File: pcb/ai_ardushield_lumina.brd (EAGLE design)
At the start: 69.8 x 53.3 mm, 90 parts, among them J1 1X02ST, J2 1X01, J3 1X06, J4 1X08, J5 1X08, J6 1X10, SW1 SW-SPST, U1 ARDUINOUNOR3-STRAIGHT

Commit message: Updated to latest libraries.  New Gerbers.
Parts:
- removed SW1: SW-SPST, Ai_Electromechanical:SPST-SMD
- added S1: SW-SPSTSMD06X06, Ai_Electromechanical:SPST-SMD06X06
- C1, C10, C11, C12, C13, C14, C15, C16, C17, C18, C19, C2, C20, C21, C22, C23, C24, C25, C26, C27, C28, C29, C3, C30, C31, C32, C33, C34, C35, C36, C37, C38, C39, C4, C40, C5, C6, C7, C8, C9: value (none) -> 0.1uF; device Ai_Passives:0603-CAP -> Ai_Passives:CAP-0603
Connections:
- net GND: now also S1.A@1, S1.A@2; no longer C38.2, SW1.A@1, SW1.A@2
- net RST: now also S1.B@1, S1.B@2; no longer SW1.B@1, SW1.B@2
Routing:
- net GND: track 532.3 -> 488.7 mm
- net RST: track 99.5 -> 91.6 mm

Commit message: Modified the routing quite a bit.
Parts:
- S1: device Ai_Electromechanical:SPST-SMD06X06 -> Ai_Electromechanical:SW-SPST-SMD06X06
- moved C13 3.43 mm to (30.4, 38.4), flipped to the top, turned to 180 degrees
- moved C10 3.43 mm to (57.1, 38.4), flipped to the top, turned to 180 degrees
- moved C11 3.43 mm to (48.3, 38.4), flipped to the top, turned to 180 degrees
- moved C12 3.43 mm to (39.4, 38.4), flipped to the top, turned to 180 degrees
- moved C14 3.43 mm to (21.6, 38.4), flipped to the top, turned to 180 degrees
- moved C15 3.43 mm to (12.7, 38.4), flipped to the top, turned to 180 degrees
- moved C16 3.43 mm to (3.81, 38.4), flipped to the top, turned to 180 degrees
- moved C9 3.43 mm to (66.0, 38.4), flipped to the top, turned to 180 degrees
- moved C17 3.30 mm to (3.81, 30.0), flipped to the top, turned to 180 degrees
- moved C18 3.30 mm to (12.7, 30.0), flipped to the top, turned to 180 degrees
- moved C19 3.30 mm to (21.6, 30.0), flipped to the top, turned to 180 degrees
- moved C20 3.30 mm to (30.5, 30.0), flipped to the top, turned to 180 degrees
- moved C21 3.30 mm to (39.4, 30.0), flipped to the top, turned to 180 degrees
- moved C22 3.30 mm to (48.3, 30.0), flipped to the top, turned to 180 degrees
- moved C23 3.30 mm to (57.1, 30.0), flipped to the top, turned to 180 degrees
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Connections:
- removed net N$47: LED8.6
- net GND: now also C38.2, LED8.6
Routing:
- net GND: track 488.7 -> 0.00 mm, vias 32 -> 0
- net VCC: track 807.9 -> 892.6 mm, vias 9 -> 40
- net N$26: track 22.3 -> 11.0 mm
- net N$8: track 21.6 -> 10.8 mm
- net N$32: track 15.3 -> 10.4 mm
- net N$16: track 15.2 -> 10.4 mm
- net N$15: track 15.2 -> 10.4 mm
- net N$14: track 15.2 -> 10.4 mm
- net N$13: track 15.2 -> 10.4 mm
- net N$11: track 15.5 -> 10.6 mm
- net N$31: track 15.2 -> 10.4 mm
- net N$29: track 15.2 -> 10.4 mm
- net N$30: track 15.2 -> 10.4 mm
- net N$33: track 15.2 -> 10.4 mm
- net N$27: track 15.5 -> 10.6 mm
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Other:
- board text added: "An Arduino Shield for a 5x8 array of WS2812 RGB LEDs."
- board text added: "C1"
- board text added: "C17"
- board text added: "C25"
- board text added: "C33"
- board text added: "C9"
- board text added: "I2C"
- board text added: "LED1"
- board text added: "LED17"
- board text added: "LED25"
- board text added: "LED33"
- board text added: "LED9"
- board text added: "RESET"
- board text added: "v1.1"
- board text removed: "(0,0)"
- board text removed: "An Arduino Shield for an 5x8 array of WS2812 RGB LEDs."
- board text removed: "RST"
- board text removed: "v1.0"

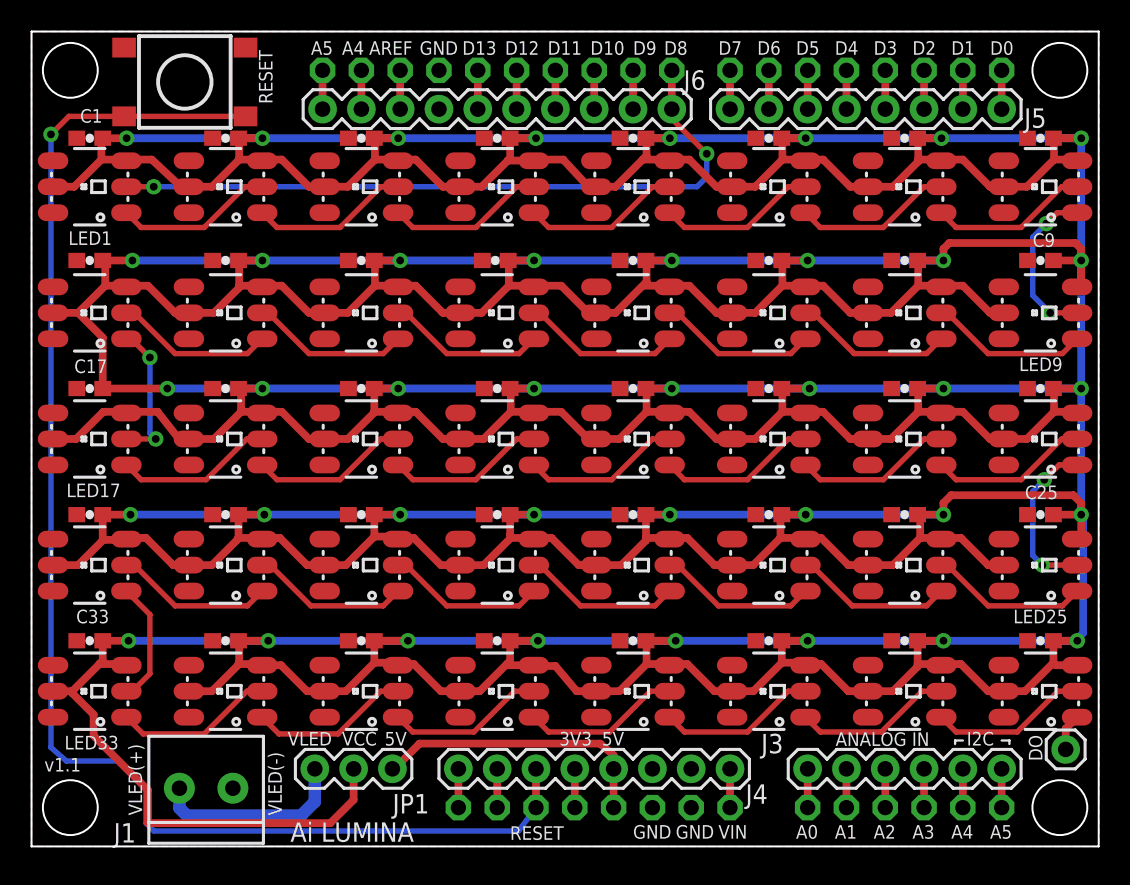
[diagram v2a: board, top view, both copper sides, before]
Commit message: Changed design to use WS2812Bs
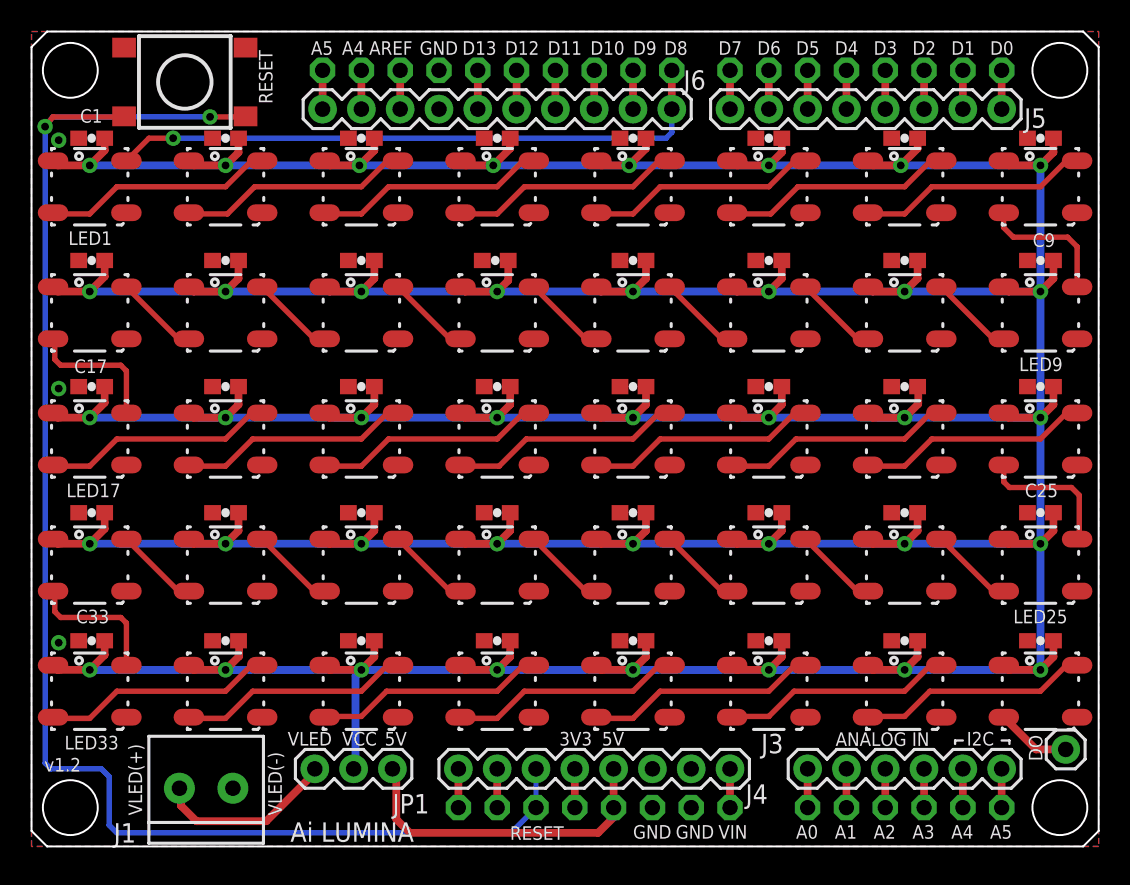
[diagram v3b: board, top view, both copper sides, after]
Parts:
- LED1, LED10, LED11, LED12, LED13, LED14, LED15, LED16, LED17, LED18, LED19, LED2, LED20, LED21, LED22, LED23, LED24, LED25, LED26, LED27, LED28, LED29, LED3, LED30, LED31, LED32, LED33, LED34, LED35, LED36, LED37, LED38, LED39, LED4, LED40, LED5, LED6, LED7, LED8, LED9: value LED-WS2812 -> LED-WS2812B; device Ai_LED:LED-WS2812 -> Ai_LED:LED-WS2812B
- moved C32 0.18 mm to (3.94, 21.8)
- moved C17 0.18 mm to (3.94, 30.1)
- moved C25 0.13 mm to (66.0, 21.8)
- moved C26 0.13 mm to (57.1, 21.8)
- moved C27 0.13 mm to (48.3, 21.8)
- moved C28 0.13 mm to (39.4, 21.8)
- moved C29 0.13 mm to (30.5, 21.8)
- moved C30 0.13 mm to (21.6, 21.8)
- moved C31 0.13 mm to (12.7, 21.8)
- moved C1 0.13 mm to (3.94, 46.4)
- moved C16 0.13 mm to (3.94, 38.4)
- moved C33 0.13 mm to (3.94, 13.5)
- moved C18 0.13 mm to (12.7, 30.1)
- moved C19 0.13 mm to (21.6, 30.1)
- moved C20 0.13 mm to (30.5, 30.1)
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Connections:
- net DI: now also LED1.4; no longer LED1.2
- net DO: now also LED40.2; no longer LED40.1
- net GND: now also LED1.3, LED10.3, LED11.3, LED12.3, LED13.3, LED14.3, LED15.3, LED16.3, LED17.3, LED18.3, LED19.3, LED2.3, LED20.3, LED21.3, LED22.3, LED23.3, LED24.3, LED25.3, LED26.3, LED27.3, LED28.3, LED29.3, LED3.3, LED30.3, LED31.3, LED32.3, LED33.3, LED34.3, LED35.3, LED36.3, LED37.3, LED38.3, LED39.3, LED4.3, LED40.3, LED5.3, LED6.3, LED7.3, LED8.3, LED9.3; no longer LED1.6, LED10.6, LED11.6, LED12.6, LED13.6, LED14.6, LED15.6, LED16.6, LED17.6, LED18.6, LED19.6, LED2.6, LED20.6, LED21.6, LED22.6, LED23.6, LED24.6, LED25.6, LED26.6, LED27.6, LED28.6, LED29.6, LED3.6, LED30.6, LED31.6, LED32.6, LED33.6, LED34.6, LED35.6, LED36.6, LED37.6, LED38.6, LED39.6, LED4.6, LED40.6, LED5.6, LED6.6, LED7.6, LED8.6, LED9.6
- net N$1: now also LED1.2, LED2.4; no longer LED1.1, LED2.2
- net N$11: now also LED10.4, LED9.2; no longer LED10.2, LED9.1
- net N$12: now also LED10.2, LED11.4; no longer LED10.1, LED11.2
- net N$13: now also LED11.2, LED12.4; no longer LED11.1, LED12.2
- net N$14: now also LED12.2, LED13.4; no longer LED12.1, LED13.2
- net N$15: now also LED13.2, LED14.4; no longer LED13.1, LED14.2
- net N$16: now also LED14.2, LED15.4; no longer LED14.1, LED15.2
- net N$17: now also LED15.2, LED16.4; no longer LED15.1, LED16.2
- net N$18: now also LED16.2, LED17.4; no longer LED16.1, LED17.2
- net N$19: now also LED17.2, LED18.4; no longer LED17.1, LED18.2
- net N$2: now also LED2.2, LED3.4; no longer LED2.1, LED3.2
- net N$20: now also LED18.2, LED19.4; no longer LED18.1, LED19.2
- net N$21: now also LED19.2, LED20.4; no longer LED19.1, LED20.2
- net N$22: now also LED20.2, LED21.4; no longer LED20.1, LED21.2
- net N$23: now also LED21.2, LED22.4; no longer LED21.1, LED22.2
- net N$24: now also LED22.2, LED23.4; no longer LED22.1, LED23.2
- net N$25: now also LED23.2, LED24.4; no longer LED23.1, LED24.2
- net N$26: now also LED24.2, LED25.4; no longer LED24.1, LED25.2
- net N$27: now also LED25.2, LED26.4; no longer LED25.1, LED26.2
- net N$28: now also LED26.2, LED27.4; no longer LED26.1, LED27.2
- net N$29: now also LED27.2, LED28.4; no longer LED27.1, LED28.2
- net N$3: now also LED3.2, LED4.4; no longer LED3.1, LED4.2
- net N$30: now also LED28.2, LED29.4; no longer LED28.1, LED29.2
- net N$31: now also LED29.2, LED30.4; no longer LED29.1, LED30.2
- net N$32: now also LED30.2, LED31.4; no longer LED30.1, LED31.2
- net N$33: now also LED31.2, LED32.4; no longer LED31.1, LED32.2
- net N$34: now also LED32.2, LED33.4; no longer LED32.1, LED33.2
- net N$35: now also LED33.2, LED34.4; no longer LED33.1, LED34.2
- net N$36: now also LED34.2, LED35.4; no longer LED34.1, LED35.2
- net N$38: now also LED35.2, LED36.4; no longer LED35.1, LED36.2
- net N$4: now also LED4.2, LED5.4; no longer LED4.1, LED5.2
- net N$40: now also LED36.2, LED37.4; no longer LED36.1, LED37.2
- net N$5: now also LED5.2, LED6.4; no longer LED5.1, LED6.2
- net N$6: now also LED6.2, LED7.4; no longer LED6.1, LED7.2
- net N$7: now also LED7.2, LED8.4; no longer LED7.1, LED8.2
- net N$74: now also LED37.2, LED38.4; no longer LED37.1, LED38.2
- net N$75: now also LED38.2, LED39.4; no longer LED38.1, LED39.2
- net N$77: now also LED39.2, LED40.4; no longer LED39.1, LED40.2
- net N$8: now also LED8.2, LED9.4; no longer LED8.1, LED9.2
- net VCC: now also LED1.1, LED10.1, LED11.1, LED12.1, LED13.1, LED14.1, LED15.1, LED16.1, LED17.1, LED18.1, LED19.1, LED2.1, LED20.1, LED21.1, LED22.1, LED23.1, LED24.1, LED25.1, LED26.1, LED27.1, LED28.1, LED29.1, LED3.1, LED30.1, LED31.1, LED32.1, LED33.1, LED34.1, LED35.1, LED36.1, LED37.1, LED38.1, LED39.1, LED4.1, LED40.1, LED5.1, LED6.1, LED7.1, LED8.1, LED9.1; no longer LED1.3, LED1.5, LED10.3, LED10.5, LED11.3, LED11.5, LED12.3, LED12.5, LED13.3, LED13.5, LED14.3, LED14.5, LED15.3, LED15.5, LED16.3, LED16.5, LED17.3, LED17.5, LED18.3, LED18.5, LED19.3, LED19.5, LED2.3, LED2.5, LED20.3, LED20.5, LED21.3, LED21.5, LED22.3, LED22.5, LED23.3, LED23.5, LED24.3, LED24.5, LED25.3, LED25.5, LED26.3, LED26.5, LED27.3, LED27.5, LED28.3, LED28.5, LED29.3, LED29.5, LED3.3, LED3.5, LED30.3, LED30.5, LED31.3, LED31.5, LED32.3, LED32.5, LED33.3, LED33.5, LED34.3, LED34.5, LED35.3, LED35.5, LED36.3, LED36.5, LED37.3, LED37.5, LED38.3, LED38.5, LED39.3, LED39.5, LED4.3, LED4.5, LED40.3, LED40.5, LED5.3, LED5.5, LED6.3, LED6.5, LED7.3, LED7.5, LED8.3, LED8.5, LED9.3, LED9.5
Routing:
- net VCC: track 892.6 -> 544.2 mm
- net RST: track 92.0 -> 99.7 mm, vias 1 -> 2
- net DI: track 46.2 -> 40.5 mm, vias 2 -> 1
- net N$27: track 10.6 -> 5.50 mm
- net N$11: track 10.6 -> 5.50 mm
- net N$31: track 10.4 -> 5.50 mm
- net N$28: track 10.4 -> 5.50 mm
- net N$30: track 10.4 -> 5.50 mm
- net N$33: track 10.4 -> 5.50 mm
- net N$15: track 10.4 -> 5.50 mm
- net N$32: track 10.4 -> 5.50 mm
- net N$29: track 10.4 -> 5.50 mm
- net N$17: track 10.4 -> 5.50 mm
- net N$14: track 10.4 -> 5.50 mm
- net N$12: track 10.4 -> 5.50 mm
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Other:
- outline, holes or cut-outs redrawn
- board text added: "An Arduino Shield for a 5x8 array of WS2812B RGB LEDs."
- board text added: "v1.2"
- board text removed: "An Arduino Shield for a 5x8 array of WS2812 RGB LEDs."
- board text removed: "v1.1"
